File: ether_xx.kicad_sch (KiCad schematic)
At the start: 46 parts, among them J6 RJ45_LED_Shielded, J7 RJ45_LED_Shielded, U10 RTL8201F, U9 RTL8201F

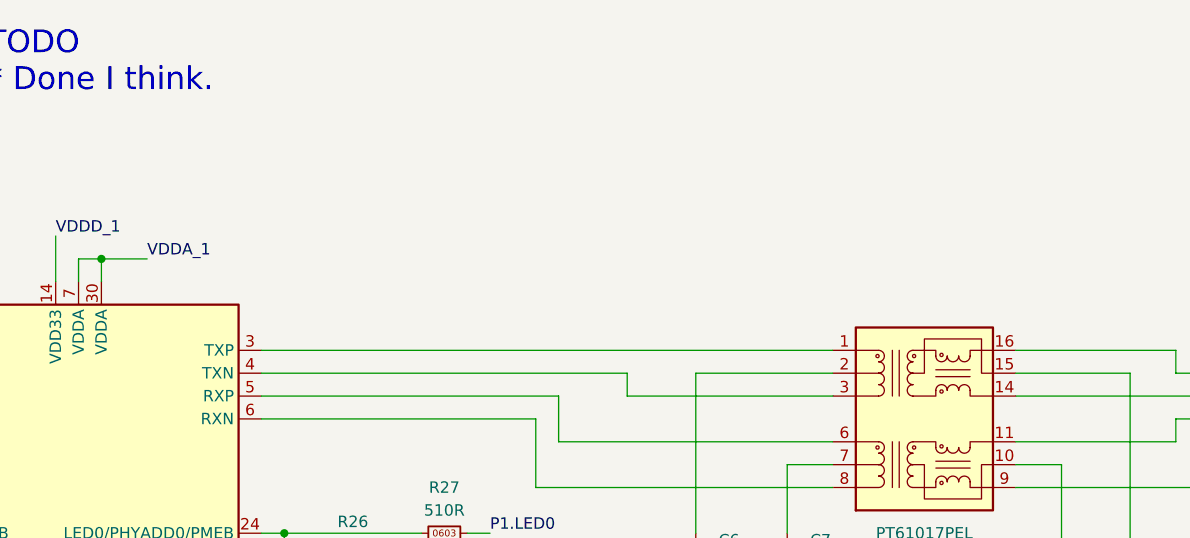
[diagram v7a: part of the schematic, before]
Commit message: start pcb?
already twisted to hell.  must be another choice for phy routing...
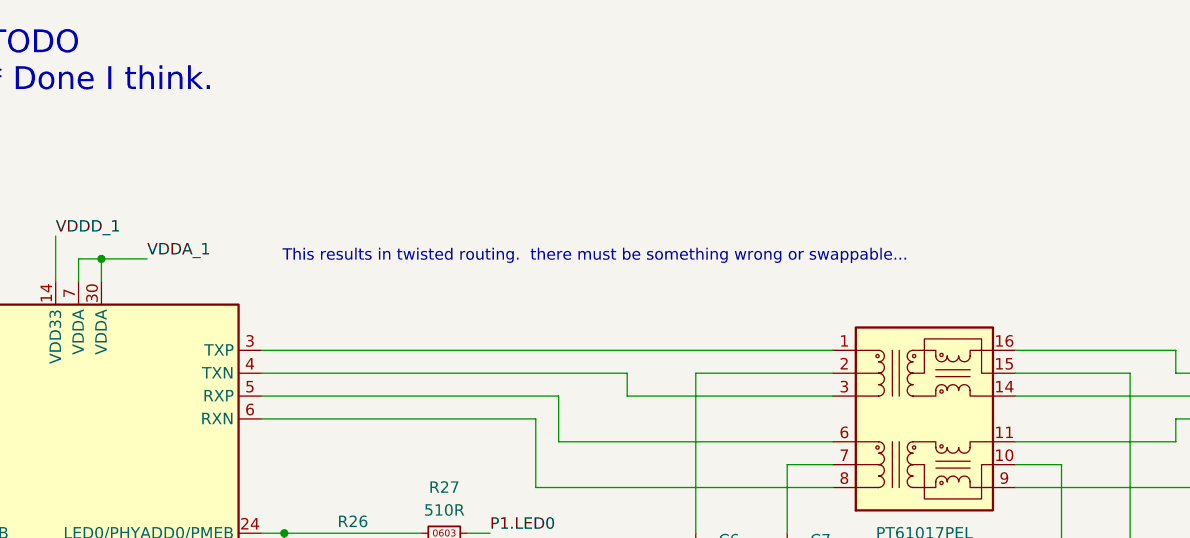
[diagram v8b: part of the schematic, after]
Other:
- note added: "This results in twisted routing. there must be something wrong or swappable..."
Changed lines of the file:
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@@
+		)
+	)
+	(text "This results in twisted routing.  there must be something wrong or swappable..."
+		(exclude_from_sim no)
+		(at 176.784 55.626 0)
+		(effects
+			(font
+				(size 1.27 1.27)
+			)
 		)
 	)
